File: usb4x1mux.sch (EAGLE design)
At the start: 43 parts, among them IC10 SN74LVC1G139DCTR, IC3 LDO5-3.3-SOT23, U1 LPC812M101JDH16

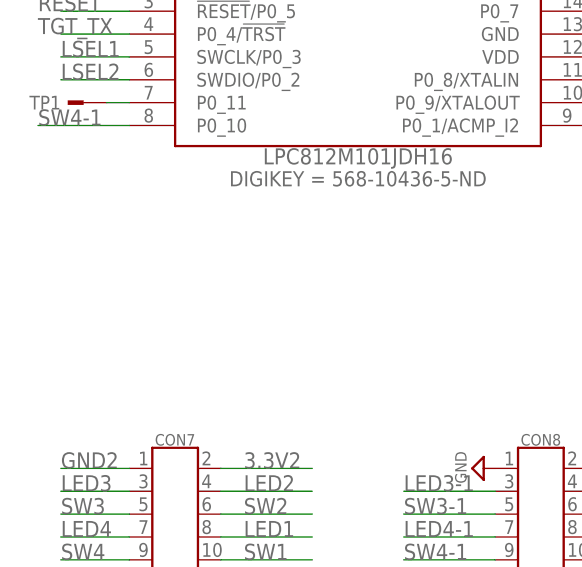
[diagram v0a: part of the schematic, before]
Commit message: update schematic
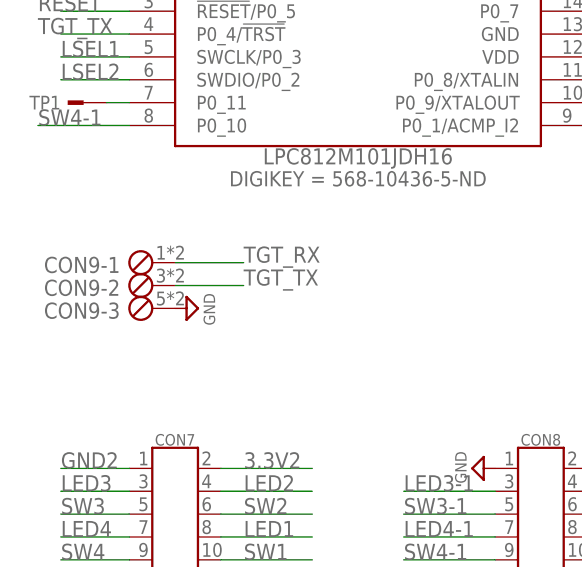
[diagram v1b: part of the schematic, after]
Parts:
- added CON9: (no value), mylib:CON-TANSHI3
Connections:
- net GND: now also CON9-3.1
- net TGT_RX: now also CON9-1.1
- net TGT_TX: now also CON9-2.1
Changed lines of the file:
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@@
 <part name="SUPPLY33" library="mylib" deviceset="GND" device=""/>
 <part name="C7" library="mylib" deviceset="C-SMD-*" device="-1608" technology="0.1U" value="0.1u/1005"/>
+<part name="CON9" library="mylib" deviceset="CON-TANSHI3" device=""/>
+<part name="SUPPLY19" library="mylib" deviceset="GND" device=""/>
 </parts>
 <sheets>
@@
 <instance part="SUPPLY33" gate="GND" x="203.2" y="58.42" rot="R90"/>
 <instance part="C7" gate="G$1" x="198.12" y="60.96"/>
+<instance part="CON9" gate="-1" x="20.32" y="83.82" rot="R180"/>
+<instance part="CON9" gate="-2" x="20.32" y="81.28" rot="R180"/>
+<instance part="CON9" gate="-3" x="20.32" y="78.74" rot="R180"/>
+<instance part="SUPPLY19" gate="GND" x="25.4" y="78.74" rot="R90"/>
 </instances>
 <busses>
@@
 <wire x1="198.12" y1="58.42" x2="195.58" y2="58.42" width="0.1524" layer="91"/>
 <junction x="198.12" y="58.42"/>
+</segment>
+<segment>
+<pinref part="CON9" gate="-3" pin="1"/>
+<pinref part="SUPPLY19" gate="GND" pin="GND"/>
 </segment>
 </net>
@@
 <label x="76.2" y="116.84" size="1.778" layer="95"/>
 </segment>
+<segment>
+<wire x1="22.86" y1="83.82" x2="30.48" y2="83.82" width="0.1524" layer="91"/>
+<pinref part="CON9" gate="-1" pin="1"/>
+<label x="30.48" y="83.82" size="1.778" layer="95"/>
+</segment>
 </net>
 <net name="ISP" class="0">
@@
 <label x="7.62" y="109.22" size="1.778" layer="95"/>
 </segment>
-</net>
+<segment>
+<wire x1="30.48" y1="81.28" x2="22.86" y2="81.28" width="0.1524" layer="91"/>
+<label x="30.48" y="81.28" size="1.778" layer="95"/>
+<pinref part="CON9" gate="-2" pin="1"/>
+</segment>
+</net>

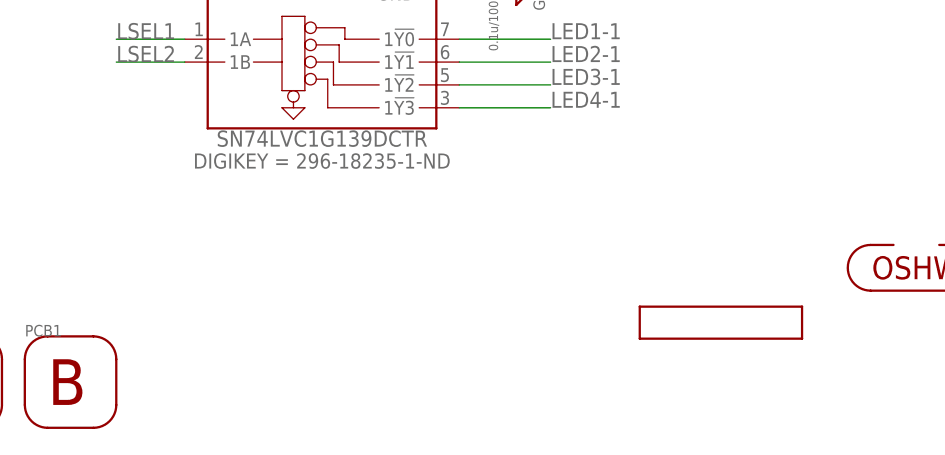
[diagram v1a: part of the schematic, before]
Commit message: update library; move git hash tag silk
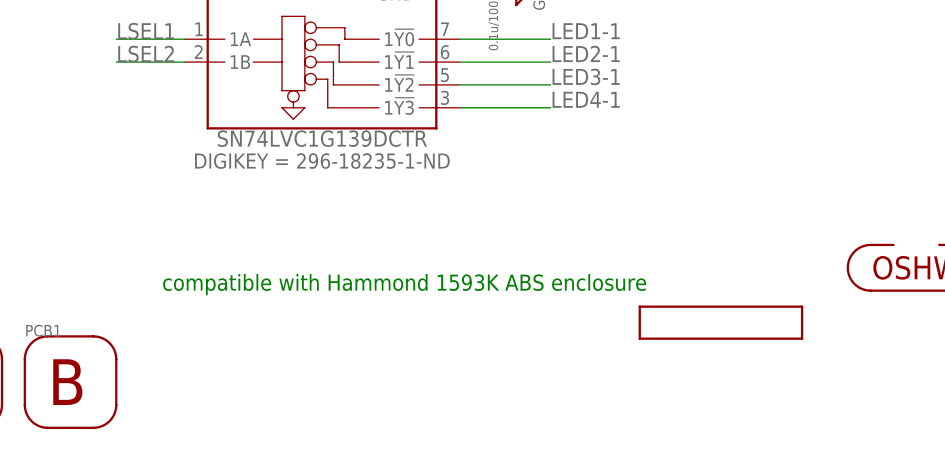
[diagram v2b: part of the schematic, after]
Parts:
- U1: device mylib:IC_LPC81X_16_JDH16 -> mylib:IC-LPC81X-16-JDH16
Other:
- note added: "compatible with Hammond 1593K ABS enclosure"
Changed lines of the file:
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@@
 <part name="SUPPLY15" library="mylib" deviceset="GND" device=""/>
 <part name="SUPPLY16" library="mylib" deviceset="GND" device=""/>
-<part name="U1" library="mylib" deviceset="IC_LPC81X_16" device="_JDH16" value="LPC812M101JDH16"/>
+<part name="U1" library="mylib" deviceset="IC-LPC81X-16" device="-JDH16" value="LPC812M101JDH16"/>
 <part name="C13" library="mylib" deviceset="C-SMD-*" device="-1608" technology="0.1U" value="0.1u/1005"/>
 <part name="SUPPLY17" library="mylib" deviceset="GND" device=""/>
@@
 1B = P0_2
 </text>
+<text x="162.56" y="25.4" size="1.778" layer="91">compatible with Hammond 1593K ABS enclosure</text>
 </plain>
 <instances>
